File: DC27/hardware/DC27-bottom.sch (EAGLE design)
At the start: 86 parts, among them IC2 LDL112D33R, IC3 FT2232HL-REEL, IC4 93LC46BT-I_OT, J1 DN PAIR, J2 JTAG, J3 Battery, U2 ESP-WROOM-32, Y1 ABM7-12.000MHZ-D2Y-T

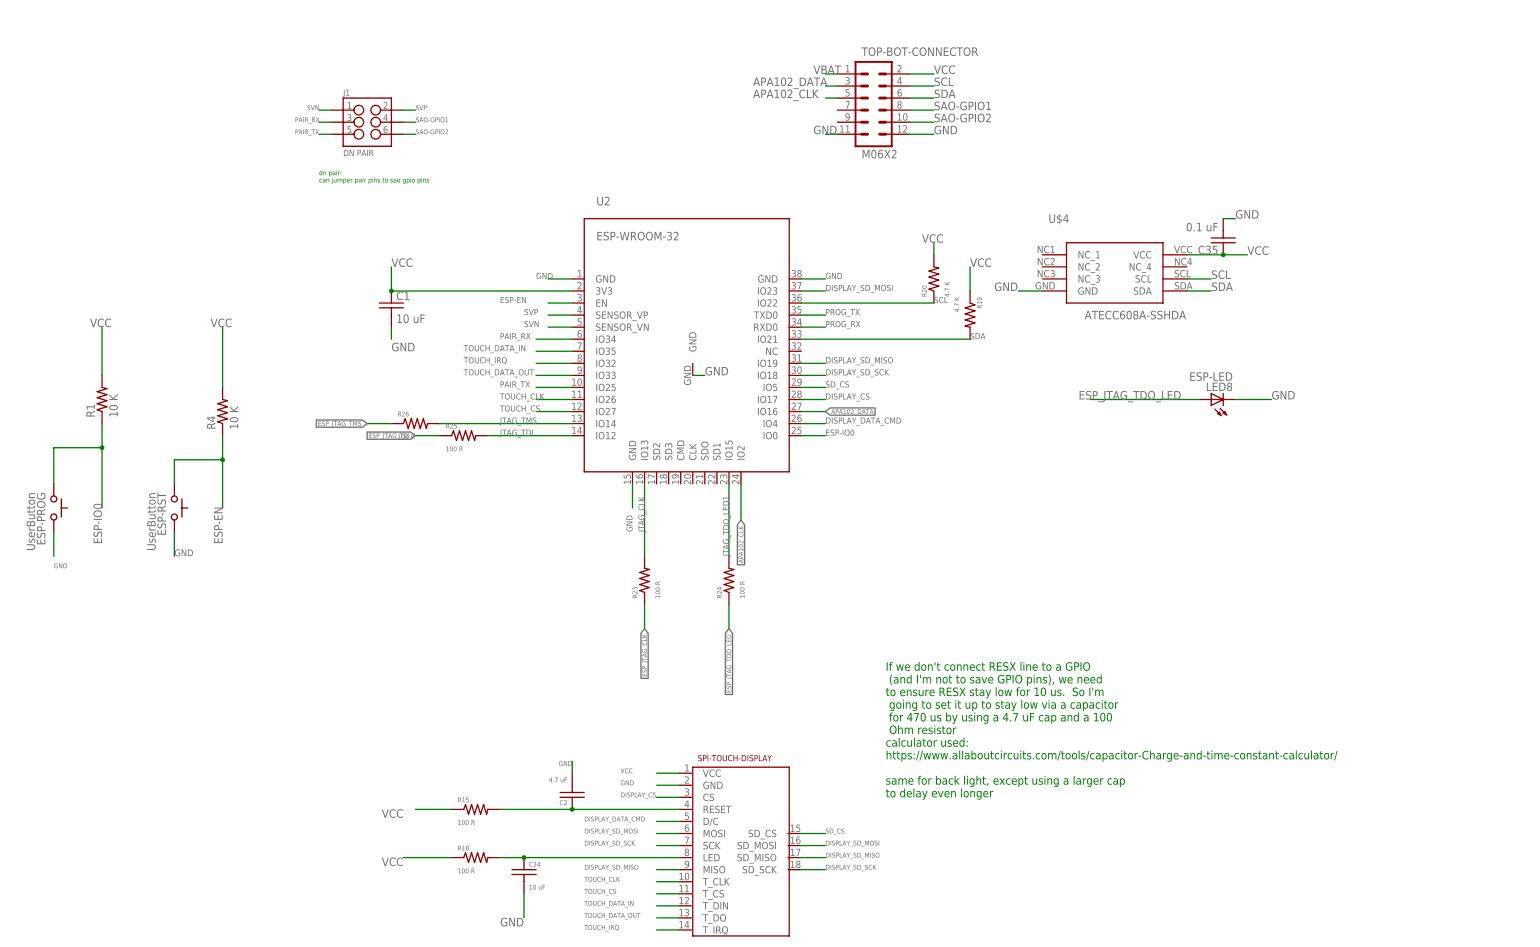
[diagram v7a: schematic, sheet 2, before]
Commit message: removed apa 102s from top board swapped led driver for atmega4089 put on programming pads bottom board adding paring headers on bottom board added 1206 56 OHM resistors to each LED top board pulled out UPDI pin on top board for programming the atmega chip
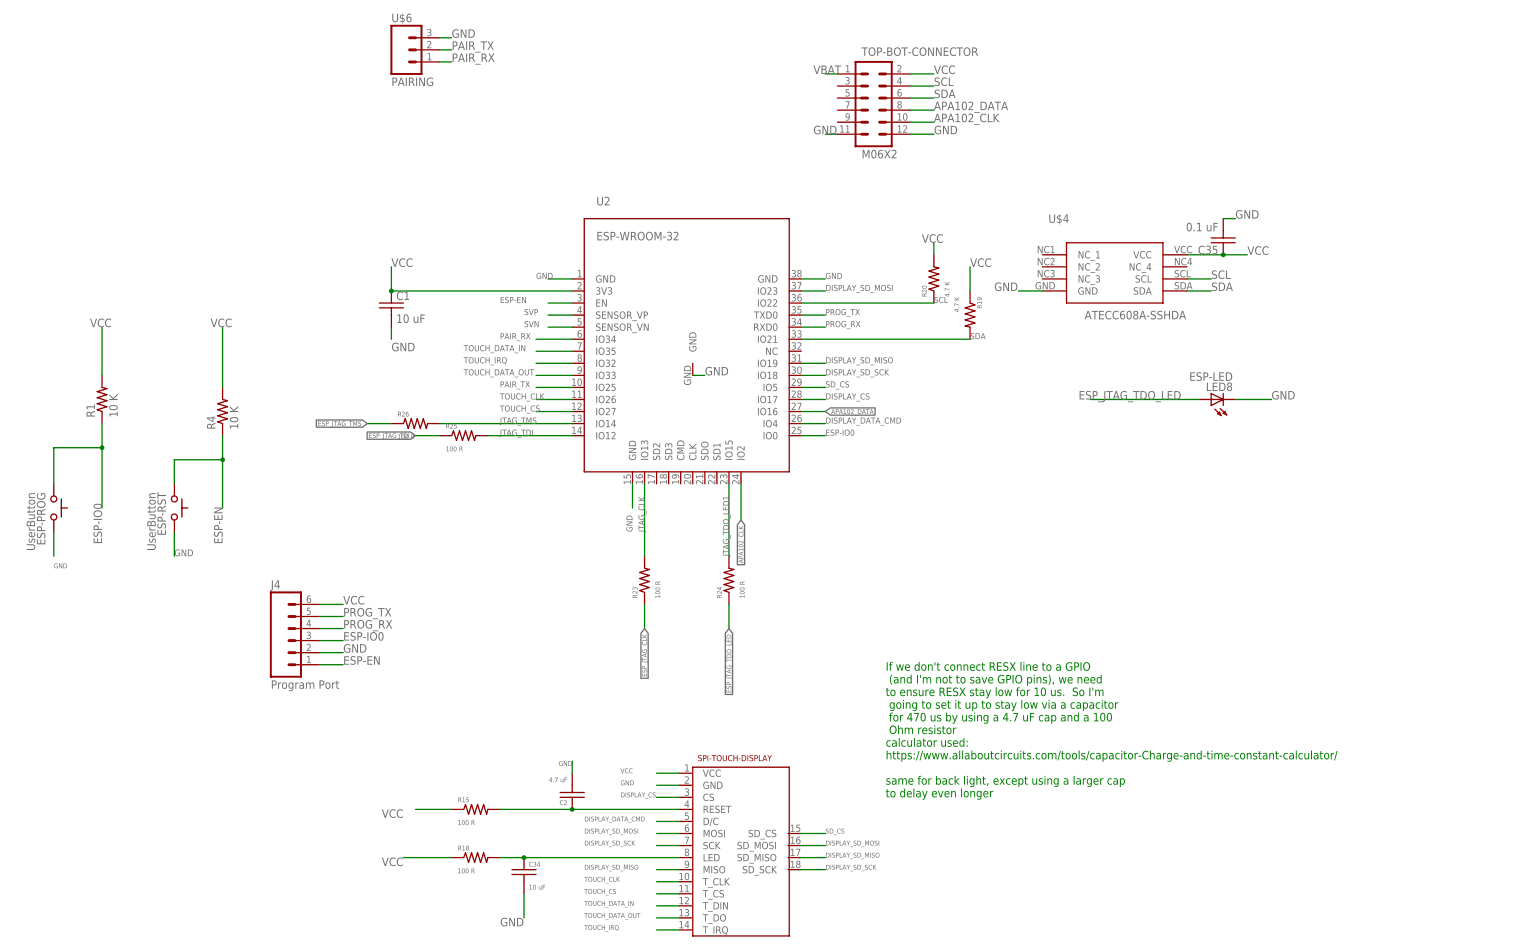
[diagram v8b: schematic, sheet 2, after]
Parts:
- removed J1: DN PAIR, connector:M03X22X3_SILK_MALE_PTH
- removed OFF/ON: Brd Power, switches:SWITCH-SPSTKIT
- added J4: Program Port, connector:M06POGO-PIN
- added PWR: MSS3-V-T_R, switches:MSS3-V-T_R
- added U$6: PAIRING, connector:M03PTH
- R3: value 10 R -> 1 K
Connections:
- removed net N$2: IC2.EN, OFF/ON.P
- removed net SAO-GPIO1: J1.4, TOP-BOT-CONNECTOR.8
- removed net SAO-GPIO2: J1.6, TOP-BOT-CONNECTOR.10
- new net EN: IC2.EN, PWR.COM
- net APA102_CLK: now also TOP-BOT-CONNECTOR.10; no longer TOP-BOT-CONNECTOR.5
- net APA102_DATA: now also TOP-BOT-CONNECTOR.8; no longer TOP-BOT-CONNECTOR.3
- net ESP-EN: now also J4.1
- net ESP-IO0: now also J4.3
- net GND: now also J4.2, PWR.GND, U$6.3; no longer OFF/ON.O
- net PAIR_RX: now also U$6.1; no longer J1.3
- net PAIR_TX: now also U$6.2; no longer J1.5
- net PROG_RX: now also J4.4
- net PROG_TX: now also J4.5
- net SVN: no longer J1.1
- net SVP: no longer J1.2
- net VBAT: now also PWR.NO; no longer OFF/ON.S
- net VCC: now also J4.6
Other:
- note removed: "dn pair: can jumper pair pins to sao gpio pins"
